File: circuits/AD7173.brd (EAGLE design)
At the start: 20.9 x 30.7 mm, 17 parts, among them IC1 AD7173, IC2 LM3485, IC3 LM3485

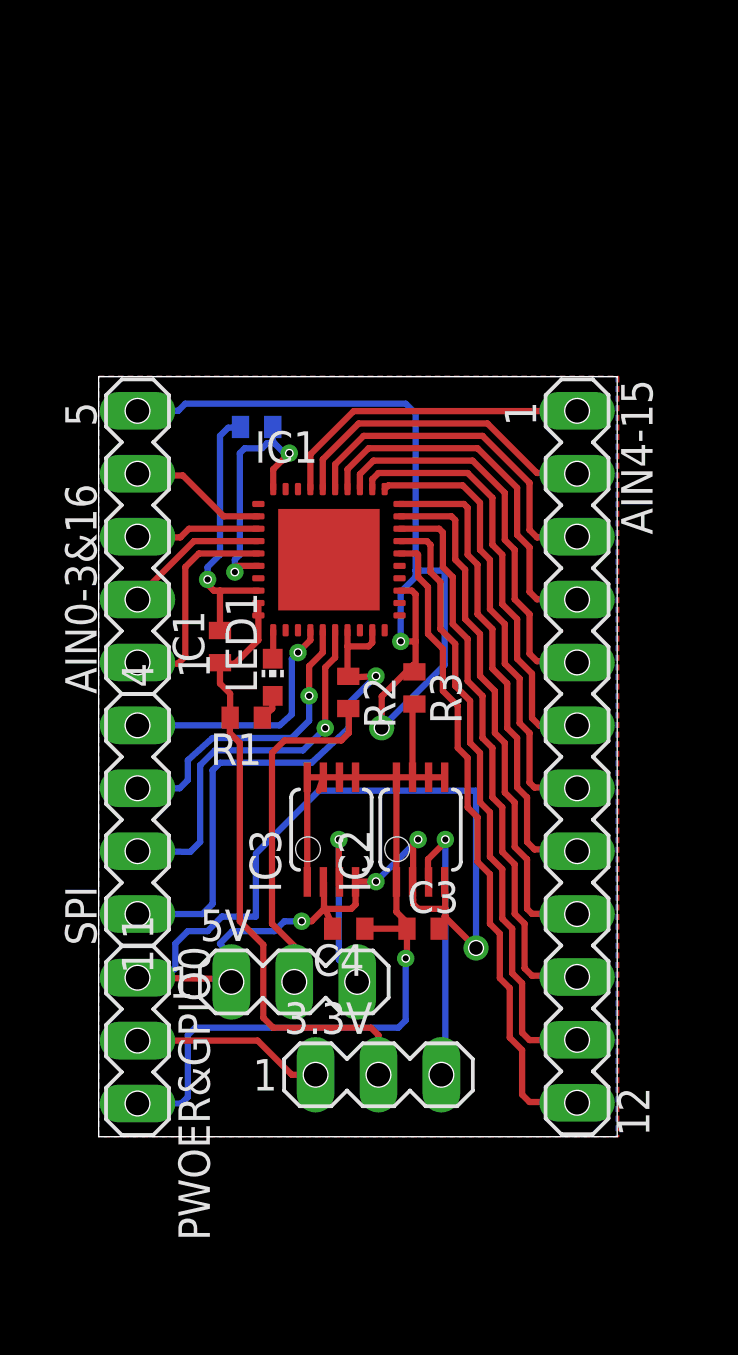
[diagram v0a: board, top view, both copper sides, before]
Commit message: circuits/* updated eagle circuits
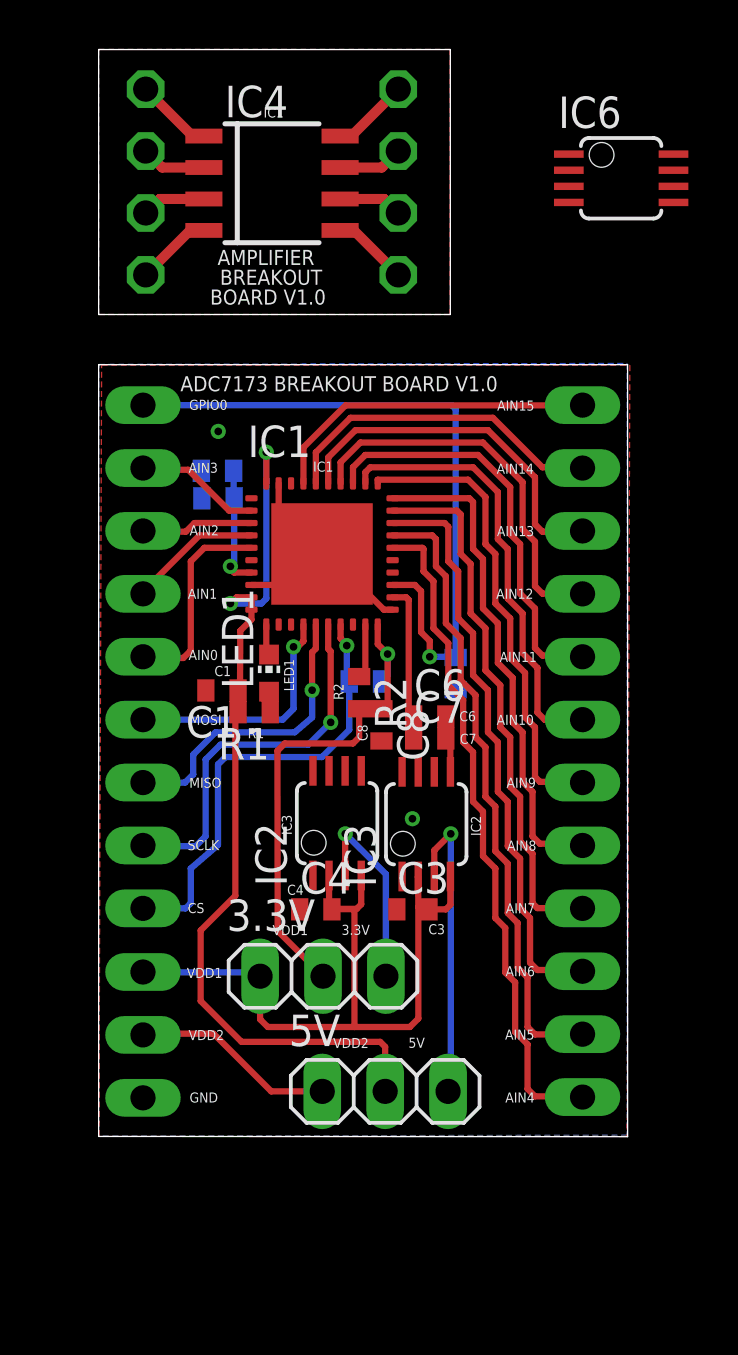
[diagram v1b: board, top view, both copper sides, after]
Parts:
- removed AIN0-3&16: (no value), con-lstb:MA05-1
- removed PWOER&GPIO0: (no value), con-lstb:MA03-1
- added AIN0-3GPIO0: (no value), pinhead:1X05
- added C5, C6, C7, C8: 0.1uF, rcl:C0402
- added IC4: OPA2134D, linear:SOIC8
- added IC6: OPA2725DGK, linear:MSOP08
- added JP1, JP2, JP3, JP4, JP5, JP6, JP7, JP8: (no value), pinhead:1X01
- added POWER: (no value), pinhead:1X03
- added R4: 10k, rcl:R0402
- 3.3V, 5V: device con-lstb:MA03-1 -> pinhead:1X03
- AIN4-15: device con-lstb:MA12-1 -> pinhead:1X12
- IC2: value LM3485 -> ADP1720; device linear:MSOP08 -> AD7173:MSOP08
- IC3: value LM3485 -> ADP1720ARMZ-5; device linear:MSOP08 -> AD7173:MSOP08
- SPI: device con-lstb:MA04-1 -> pinhead:1X04
- moved 5V 5.75 mm to (11.6, 1.83)
- moved 3.3V 4.57 mm to (9.06, 6.48)
- moved IC3 3.84 mm to (13.2, 12.6)
- moved IC2 3.38 mm to (9.63, 12.7)
- moved C2 2.37 mm to (4.80, 26.9)
- moved C1 1.77 mm to (4.98, 18.0), turned to 180 degrees
- moved R3 1.77 mm to (14.4, 18.7), flipped to the bottom
- moved C4 1.54 mm to (8.77, 9.18), turned to 0 degrees
- moved C3 0.88 mm to (12.7, 9.18)
- moved R2 0.44 mm to (10.5, 17.9)
- moved R1 0.39 mm to (6.28, 17.1)
- moved IC1 0.36 mm to (9.02, 23.5)
- moved AIN4-15 0.32 mm to (19.5, 15.6), flipped to the bottom
- moved SPI 0.32 mm to (1.79, 13.0), flipped to the bottom
- moved LED1 0.23 mm to (6.88, 18.7)
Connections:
- removed net AIN16: IC1.1
- removed net DGND: IC1.21
- removed net GPIO1: IC1.24
- removed net GPIO2: IC1.25
- removed net REF-: IC1.39
- removed net REGCAPD: IC1.22
- new net N$28: 3.3V.1, C3.2, C4.2, IC2.2, IC2.4, IC3.2, IC3.4, POWER.1
- new net N$30: 5V.3, IC3.3
- new net N$31: IC4.1, JP1.1
- new net N$33: IC4.2, JP2.1
- new net N$34: IC4.3, JP3.1
- new net N$35: IC4.4, JP4.1
- new net N$36: IC4.5, JP5.1
- new net N$37: IC4.6, JP6.1
- new net N$38: C6.1, C7.1, IC1.22
- new net N$39: IC1.19, R2.1
- new net N$40: IC4.7, JP7.1
- new net N$41: IC4.8, JP8.1
- new net V+: IC6.8
- new net V-: IC6.4
- net +3V3: now also 3.3V.2, C8.1, IC1.20, R4.2; no longer 5V.2
- net +5V: now also 5V.2, IC1.40; no longer 3.3V.2
- net GND: now also C5.1, C6.2, C7.2, C8.2, IC1.21, IC1.39, IC1.41, POWER.3; no longer PWOER&GPIO0.3
- net N$18: now also AIN0-3GPIO0.1; no longer AIN0-3&16.1
- net N$19: now also AIN0-3GPIO0.2; no longer AIN0-3&16.2
- net N$20: now also AIN0-3GPIO0.3; no longer AIN0-3&16.3
- net N$21: now also AIN0-3GPIO0.4; no longer AIN0-3&16.4
- net N$22: now also 5V.1, POWER.2; no longer 3.3V.1, PWOER&GPIO0.2
- net N$27: now also 3.3V.3, IC2.3; no longer 5V.1, C3.2, C4.2, IC2.2, IC2.4, IC3.2, IC3.4, PWOER&GPIO0.1
- net N$3: now also R4.1; no longer IC1.19, R2.1
- net N$5: now also AIN0-3GPIO0.5; no longer AIN0-3&16.5
- net N$6: now also C5.2, IC1.7; no longer IC1.40, IC1.6
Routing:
- net N$27: track 50.0 -> 8.12 mm
- net GND: track 49.7 -> 13.4 mm, vias 1 -> 2
- net N$28: track 0.00 -> 31.1 mm, vias 1 -> 0
- net N$30: track 0.00 -> 12.4 mm
- net +5V: track 25.1 -> 37.1 mm, vias 0 -> 2
- net N$26: track 11.5 -> 0.00 mm, vias 1 -> 0
- net N$5: track 37.3 -> 27.8 mm
- net N$2: track 7.88 -> 0.00 mm, vias 1 -> 0
- net +3V3: track 14.1 -> 20.5 mm, vias 0 -> 1
- net N$38: track 0.00 -> 6.37 mm
- net N$6: track 10.6 -> 5.00 mm, vias 0 -> 1
- net N$3: track 21.9 -> 18.4 mm, vias 0 -> 1
- net N$41: track 0.00 -> 3.13 mm
- net N$31: track 0.00 -> 3.13 mm, vias 1 -> 0
- net N$35: track 0.00 -> 3.09 mm, vias 1 -> 0
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- added copper zone on layer 1, net N$42
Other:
- board size 20.9 x 30.7 mm -> 21.4 x 43.9 mm
- board text added: "ADC7173 BREAKOUT BOARD V1.0"
- board text added: "AMPLIFIER"
- board text added: "BOARD V1.0"
- board text added: "BREAKOUT"
- board text added: "C5"
- board text added: "C6"
- board text added: "C7"
- board text added: "C8"
- board text added: "R4"
- board text removed: "DIRECT"
